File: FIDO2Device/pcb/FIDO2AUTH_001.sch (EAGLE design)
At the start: 1 part, among them U1 MDBT50Q-P1M

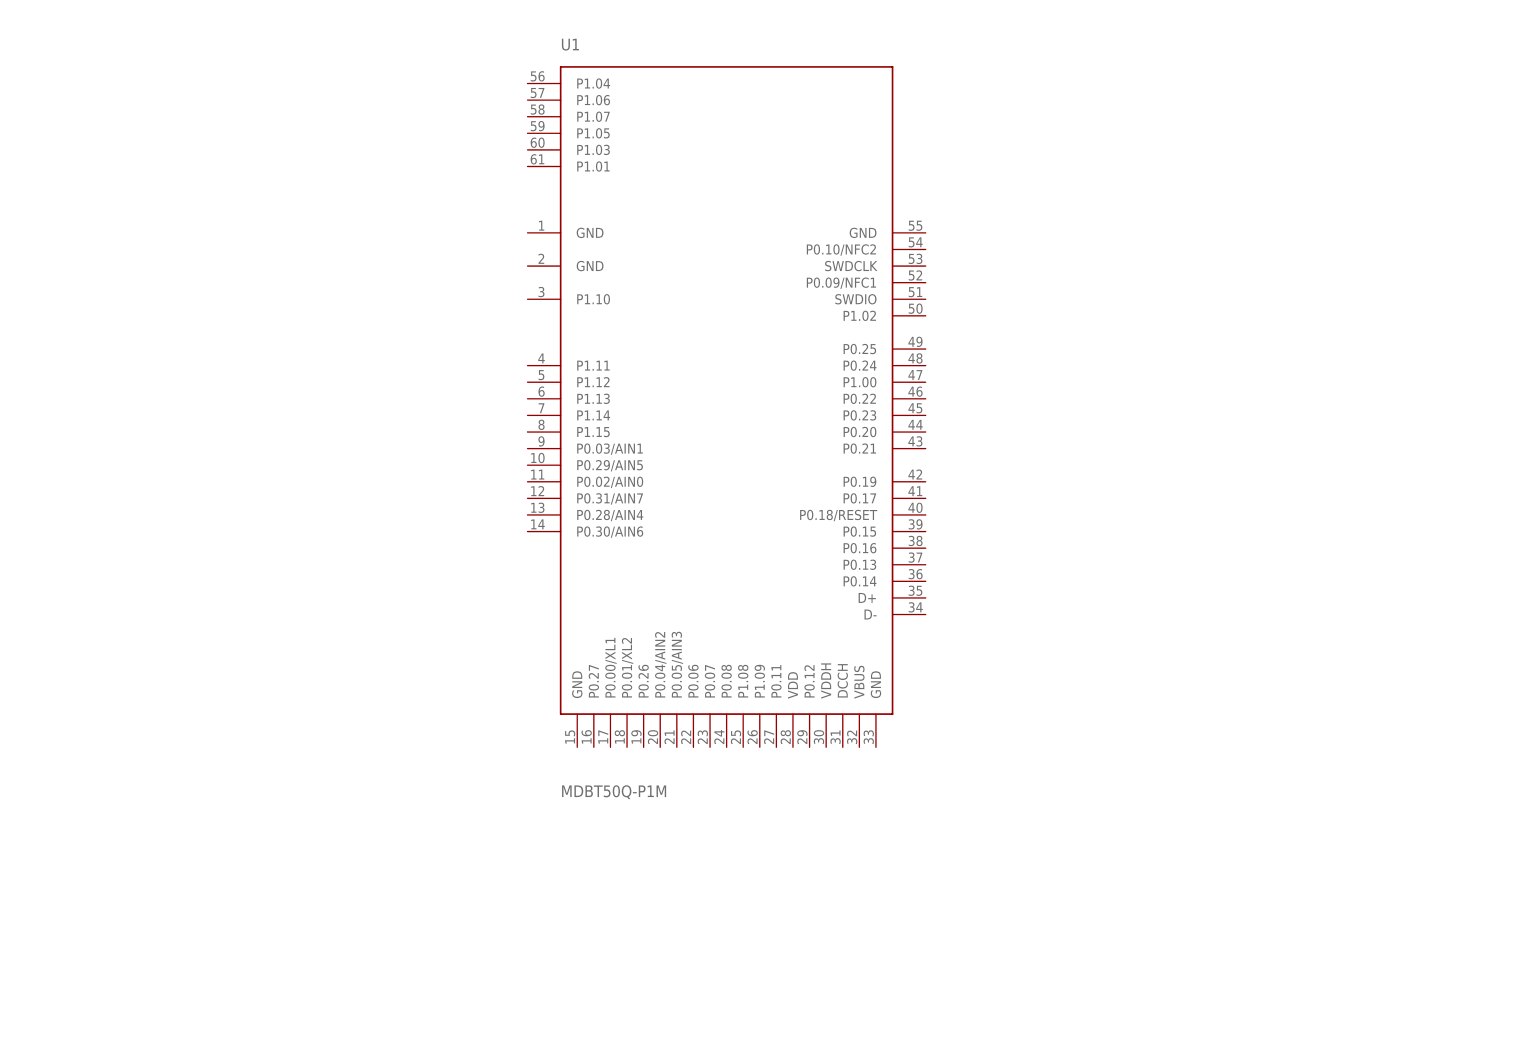
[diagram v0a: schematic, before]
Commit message: [WIP] ブレークアウト基板回路図
・クリスタル、バイパスコンデンサーを追加配置
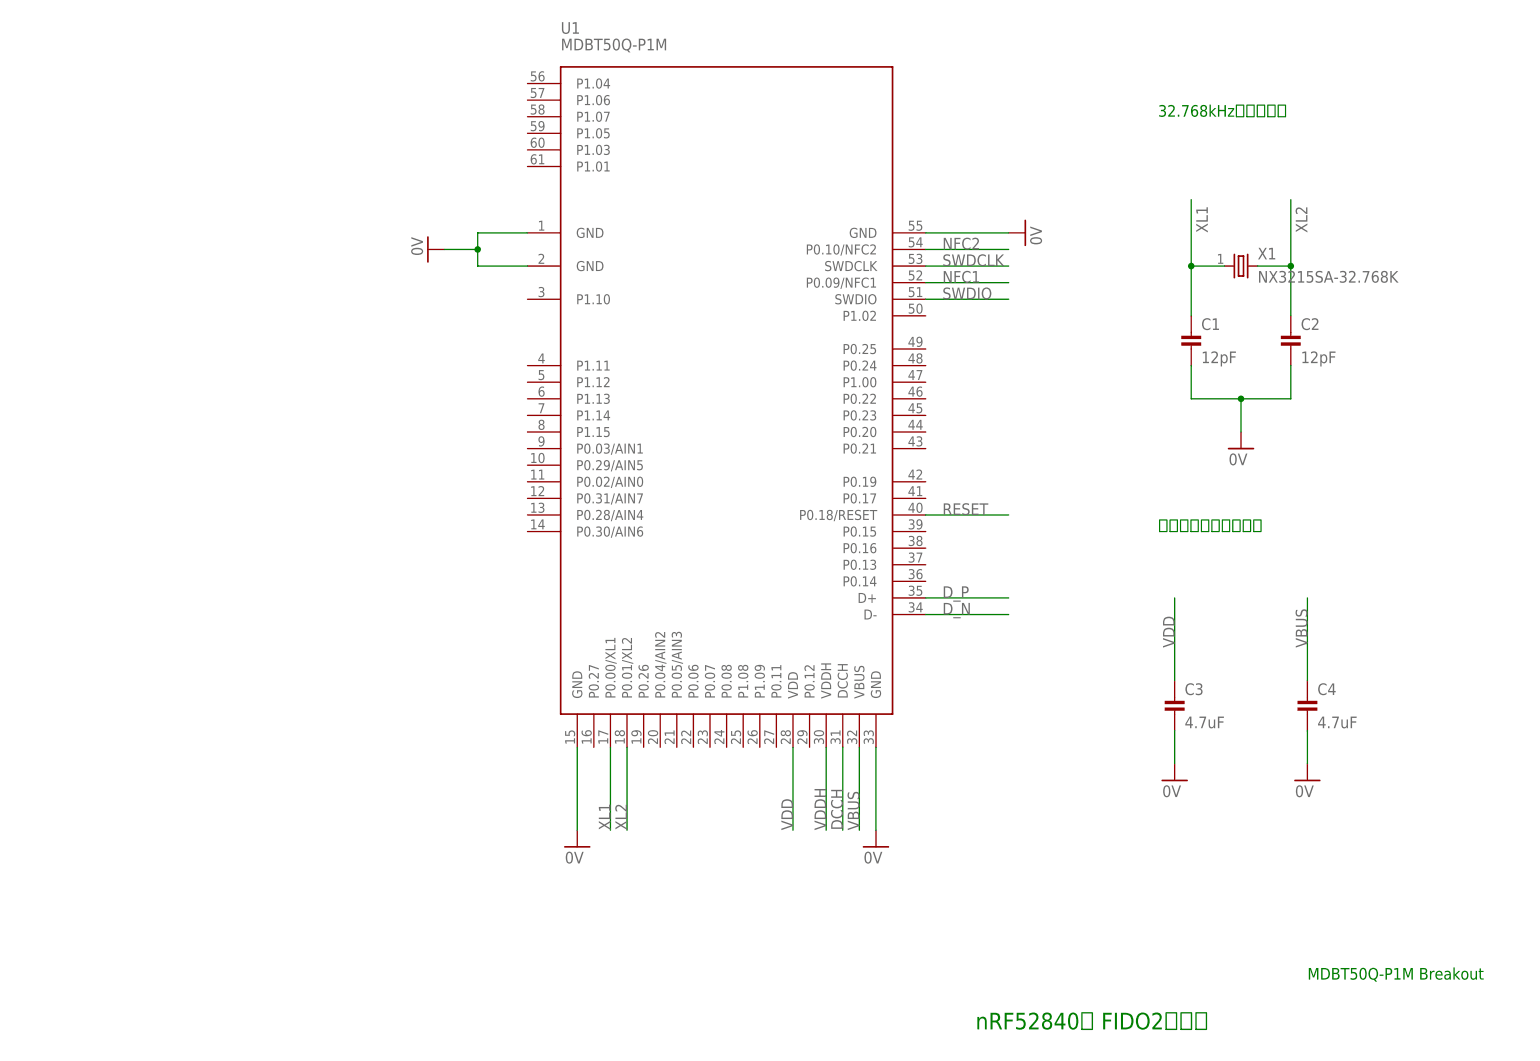
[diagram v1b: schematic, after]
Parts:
- added C1, C2: 12pF, Parts:CAP_0603
- added C3, C4: 4.7uF, Parts:CAP_0603
- added X1: NX3215SA-32.768K, Parts:NX3215SA-32.768K
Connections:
- new net 0V: C1.2, C2.2, C3.2, C4.2, U1.GND@1, U1.GND@15, U1.GND@2, U1.GND@33, U1.GND@55
- new net DCCH: U1.DCCH
- new net D_N: U1.D-
- new net D_P: U1.D+
- new net NFC1: U1.P0.09/NFC1
- new net NFC2: U1.P0.10/NFC2
- new net RESET: U1.P0.18/RESET
- new net SWDCLK: U1.SWDCLK
- new net SWDIO: U1.SWDIO
- new net VBUS: C4.1, U1.VBUS
- new net VDD: C3.1, U1.VDD
- new net VDDH: U1.VDDH
- new net XL1: C1.1, U1.P0.00/XL1, X1.1
- new net XL2: C2.1, U1.P0.01/XL2, X1.2
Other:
- note added: "32.768kHzクリスタル"
- note added: "MDBT50Q-P1M Breakout"
- note added: "nRF52840版 FIDO2認証器"
- note added: "バイパスコンデンサー"
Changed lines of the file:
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@@
 <setting verticaltext="up"/>
 </settings>
-<grid distance="0.1" unitdist="inch" unit="inch" style="lines" multiple="1" display="no" altdistance="0.01" altunitdist="inch" altunit="inch"/>
+<grid distance="0.1" unitdist="inch" unit="inch" style="lines" multiple="1" display="yes" altdistance="0.01" altunitdist="inch" altunit="inch"/>
 <layers>
 <layer number="1" name="Top" color="4" fill="1" visible="no" active="no"/>
@@
 <part name="U1" library="Parts" deviceset="MDBT50Q-P1M" device=""/>
 <part name="FRAME1" library="Generic" deviceset="A4L-LOC" device=""/>
+<part name="X1" library="Parts" deviceset="NX3215SA" device="-32.768K"/>
+<part name="C1" library="Parts" deviceset="CAP" device="_0603" value="12pF"/>
+<part name="C2" library="Parts" deviceset="CAP" device="_0603" value="12pF"/>
+<part name="GND1" library="Supply" deviceset="0V" device=""/>
+<part name="C3" library="Parts" deviceset="CAP" device="_0603" value="4.7uF"/>
+<part name="C4" library="Parts" deviceset="CAP" device="_0603" value="4.7uF"/>
+<part name="GND2" library="Supply" deviceset="0V" device=""/>
+<part name="GND3" library="Supply" deviceset="0V" device=""/>
+<part name="GND4" library="Supply" deviceset="0V" device=""/>
+<part name="GND5" library="Supply" deviceset="0V" device=""/>
+<part name="GND6" library="Supply" deviceset="0V" device=""/>
+<part name="GND7" library="Supply" deviceset="0V" device=""/>
 </parts>
 <sheets>
 <sheet>
 <plain>
+<text x="195.58" y="152.4" size="1.778" layer="91">32.768kHzクリスタル</text>
+<text x="195.58" y="88.9" size="1.778" layer="91">バイパスコンデンサー</text>
+<text x="218.44" y="20.32" size="1.778" layer="91">MDBT50Q-P1M Breakout</text>
+<text x="167.64" y="12.7" size="2.54" layer="91">nRF52840版 FIDO2認証器</text>
 </plain>
 <instances>
-<instance part="U1" gate="G$1" x="129.54" y="106.68"/>
+<instance part="U1" gate="G$1" x="129.54" y="106.68" smashed="yes">
+<attribute name="NAME" x="104.14" y="165.1" size="1.778" layer="95"/>
+<attribute name="VALUE" x="104.14" y="162.56" size="1.778" layer="96"/>
+</instance>
 <instance part="FRAME1" gate="G$1" x="0" y="0"/>
+<instance part="X1" gate="G$1" x="208.28" y="129.54"/>
+<instance part="C1" gate="G$1" x="200.66" y="121.92"/>
+<instance part="C2" gate="G$1" x="215.9" y="121.92"/>
+<instance part="GND1" gate="1" x="208.28" y="101.6"/>
+<instance part="C3" gate="G$1" x="198.12" y="66.04"/>
+<instance part="C4" gate="G$1" x="218.44" y="66.04"/>
+<instance part="GND2" gate="1" x="198.12" y="50.8"/>
+<instance part="GND3" gate="1" x="218.44" y="50.8"/>
+<instance part="GND4" gate="1" x="152.4" y="40.64"/>
+<instance part="GND5" gate="1" x="175.26" y="134.62" rot="R90"/>
+<instance part="GND6" gate="1" x="83.82" y="132.08" rot="R270"/>
+<instance part="GND7" gate="1" x="106.68" y="40.64"/>
 </instances>
 <busses>
 </busses>
 <nets>
+<net name="0V" class="0">
+<segment>
+<pinref part="C1" gate="G$1" pin="2"/>
+<wire x1="200.66" y1="114.3" x2="200.66" y2="109.22" width="0.1524" layer="91"/>
+<pinref part="GND1" gate="1" pin="0V"/>
+<wire x1="200.66" y1="109.22" x2="208.28" y2="109.22" width="0.1524" layer="91"/>
+<wire x1="208.28" y1="109.22" x2="208.28" y2="104.14" width="0.1524" layer="91"/>
+<wire x1="208.28" y1="109.22" x2="215.9" y2="109.22" width="0.1524" layer="91"/>
+<junction x="208.28" y="109.22"/>
+<pinref part="C2" gate="G$1" pin="2"/>
+<wire x1="215.9" y1="109.22" x2="215.9" y2="114.3" width="0.1524" layer="91"/>
+</segment>
+<segment>
+<pinref part="GND2" gate="1" pin="0V"/>
+<pinref part="C3" gate="G$1" pin="2"/>
+<wire x1="198.12" y1="53.34" x2="198.12" y2="58.42" width="0.1524" layer="91"/>
+</segment>
+<segment>
+<pinref part="GND3" gate="1" pin="0V"/>
+<pinref part="C4" gate="G$1" pin="2"/>
+<wire x1="218.44" y1="53.34" x2="218.44" y2="58.42" width="0.1524" layer="91"/>
+</segment>
+<segment>
+<pinref part="U1" gate="G$1" pin="GND@15"/>
+<pinref part="GND7" gate="1" pin="0V"/>
+<wire x1="106.68" y1="55.88" x2="106.68" y2="43.18" width="0.1524" layer="91"/>
+</segment>
+<segment>
+<pinref part="U1" gate="G$1" pin="GND@33"/>
+<pinref part="GND4" gate="1" pin="0V"/>
+<wire x1="152.4" y1="55.88" x2="152.4" y2="43.18" width="0.1524" layer="91"/>
+</segment>
+<segment>
+<pinref part="U1" gate="G$1" pin="GND@55"/>
+<pinref part="GND5" gate="1" pin="0V"/>
+<wire x1="160.02" y1="134.62" x2="172.72" y2="134.62" width="0.1524" layer="91"/>
+</segment>
+<segment>
+<pinref part="U1" gate="G$1" pin="GND@1"/>
+<wire x1="99.06" y1="134.62" x2="91.44" y2="134.62" width="0.1524" layer="91"/>
+<wire x1="91.44" y1="134.62" x2="91.44" y2="132.08" width="0.1524" layer="91"/>
+<pinref part="GND6" gate="1" pin="0V"/>
+<wire x1="91.44" y1="132.08" x2="86.36" y2="132.08" width="0.1524" layer="91"/>
+<pinref part="U1" gate="G$1" pin="GND@2"/>
+<wire x1="99.06" y1="129.54" x2="91.44" y2="129.54" width="0.1524" layer="91"/>
+<wire x1="91.44" y1="129.54" x2="91.44" y2="132.08" width="0.1524" layer="91"/>
+<junction x="91.44" y="132.08"/>
+</segment>
+</net>
+<net name="XL1" class="0">
+<segment>
+<pinref part="X1" gate="G$1" pin="1"/>
+<wire x1="205.74" y1="129.54" x2="200.66" y2="129.54" width="0.1524" layer="91"/>
+<pinref part="C1" gate="G$1" pin="1"/>
+<wire x1="200.66" y1="129.54" x2="200.66" y2="121.92" width="0.1524" layer="91"/>
+<wire x1="200.66" y1="129.54" x2="200.66" y2="139.7" width="0.1524" layer="91"/>
+<junction x="200.66" y="129.54"/>
+<label x="203.2" y="134.62" size="1.778" layer="95" rot="R90"/>
+</segment>
+<segment>
+<pinref part="U1" gate="G$1" pin="P0.00/XL1"/>
+<wire x1="111.76" y1="55.88" x2="111.76" y2="43.18" width="0.1524" layer="91"/>
+<label x="111.76" y="43.18" size="1.778" layer="95" rot="R90"/>
+</segment>
+</net>
+<net name="XL2" class="0">
+<segment>
+<pinref part="X1" gate="G$1" pin="2"/>
+<pinref part="C2" gate="G$1" pin="1"/>
+<wire x1="210.82" y1="129.54" x2="215.9" y2="129.54" width="0.1524" layer="91"/>
+<wire x1="215.9" y1="129.54" x2="215.9" y2="121.92" width="0.1524" layer="91"/>
+<wire x1="215.9" y1="129.54" x2="215.9" y2="139.7" width="0.1524" layer="91"/>
+<junction x="215.9" y="129.54"/>
+<label x="218.44" y="134.62" size="1.778" layer="95" rot="R90"/>
+</segment>
+<segment>
+<pinref part="U1" gate="G$1" pin="P0.01/XL2"/>
+<wire x1="114.3" y1="55.88" x2="114.3" y2="43.18" width="0.1524" layer="91"/>
+<label x="114.3" y="43.18" size="1.778" layer="95" rot="R90"/>
+</segment>
+</net>
+<net name="VDD" class="0">
+<segment>
+<pinref part="C3" gate="G$1" pin="1"/>
+<wire x1="198.12" y1="66.04" x2="198.12" y2="78.74" width="0.1524" layer="91"/>
+<label x="198.12" y="71.12" size="1.778" layer="95" rot="R90"/>
+</segment>
+<segment>
+<pinref part="U1" gate="G$1" pin="VDD"/>
+<wire x1="139.7" y1="55.88" x2="139.7" y2="43.18" width="0.1524" layer="91"/>
+<label x="139.7" y="43.18" size="1.778" layer="95" rot="R90"/>
+</segment>
+</net>
+<net name="VBUS" class="0">
+<segment>
+<pinref part="C4" gate="G$1" pin="1"/>
+<wire x1="218.44" y1="66.04" x2="218.44" y2="78.74" width="0.1524" layer="91"/>
+<label x="218.44" y="71.12" size="1.778" layer="95" rot="R90"/>
+</segment>
+<segment>
+<pinref part="U1" gate="G$1" pin="VBUS"/>
+<wire x1="149.86" y1="55.88" x2="149.86" y2="43.18" width="0.1524" layer="91"/>
+<label x="149.86" y="43.18" size="1.778" layer="95" rot="R90"/>
+</segment>
+</net>
+<net name="SWDCLK" class="0">
+<segment>
+<pinref part="U1" gate="G$1" pin="SWDCLK"/>
+<wire x1="160.02" y1="129.54" x2="172.72" y2="129.54" width="0.1524" layer="91"/>
+<label x="162.56" y="129.54" size="1.778" layer="95"/>
+</segment>
+</net>
+<net name="NFC1" class="0">
+<segment>
+<pinref part="U1" gate="G$1" pin="P0.09/NFC1"/>
+<wire x1="160.02" y1="127" x2="172.72" y2="127" width="0.1524" layer="91"/>
+<label x="162.56" y="127" size="1.778" layer="95"/>
+</segment>
+</net>
+<net name="NFC2" class="0">
+<segment>
+<pinref part="U1" gate="G$1" pin="P0.10/NFC2"/>
+<wire x1="160.02" y1="132.08" x2="172.72" y2="132.08" width="0.1524" layer="91"/>
+<label x="162.56" y="132.08" size="1.778" layer="95"/>
+</segment>
+</net>
+<net name="SWDIO" class="0">
+<segment>
+<pinref part="U1" gate="G$1" pin="SWDIO"/>
+<wire x1="160.02" y1="124.46" x2="172.72" y2="124.46" width="0.1524" layer="91"/>
+<label x="162.56" y="124.46" size="1.778" layer="95"/>
+</segment>
+</net>
+<net name="RESET" class="0">
+<segment>
+<pinref part="U1" gate="G$1" pin="P0.18/RESET"/>
+<wire x1="160.02" y1="91.44" x2="172.72" y2="91.44" width="0.1524" layer="91"/>
+<label x="162.56" y="91.44" size="1.778" layer="95"/>
+</segment>
+</net>
+<net name="D_P" class="0">
+<segment>
+<pinref part="U1" gate="G$1" pin="D+"/>
+<wire x1="160.02" y1="78.74" x2="172.72" y2="78.74" width="0.1524" layer="91"/>
+<label x="162.56" y="78.74" size="1.778" layer="95"/>
+</segment>
+</net>
+<net name="D_N" class="0">
+<segment>
+<pinref part="U1" gate="G$1" pin="D-"/>
+<wire x1="160.02" y1="76.2" x2="172.72" y2="76.2" width="0.1524" layer="91"/>
+<label x="162.56" y="76.2" size="1.778" layer="95"/>
+</segment>
+</net>
+<net name="VDDH" class="0">
+<segment>
+<pinref part="U1" gate="G$1" pin="VDDH"/>
+<wire x1="144.78" y1="55.88" x2="144.78" y2="43.18" width="0.1524" layer="91"/>
+<label x="144.78" y="43.18" size="1.778" layer="95" rot="R90"/>
+</segment>
+</net>
+<net name="DCCH" class="0">
+<segment>
+<pinref part="U1" gate="G$1" pin="DCCH"/>
+<wire x1="147.32" y1="55.88" x2="147.32" y2="43.18" width="0.1524" layer="91"/>
+<label x="147.32" y="43.18" size="1.778" layer="95" rot="R90"/>
+</segment>
+</net>
 </nets>
 </sheet>

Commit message: [WIP] ブレークアウト基板回路図
・USBプラグ部を追加
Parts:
- added C5, C6: 10uF, Parts:CAP_0603
- added C7, C8: 0.1uF, Parts:CAP_0402
- added CN1: TE-1734028, Connectors:TE-1734028
- added D1: PRTR5V0U2X, Parts:PRTR5V0U2X
- added FB1, FB2, FB3: BLM15AG121SN1D, Parts:BLM15AG121SN1D
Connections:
- removed net DCCH: U1.DCCH
- removed net VBUS: C4.1, U1.VBUS
- removed net VDD: C3.1, U1.VDD
- removed net VDDH: U1.VDDH
- new net N$1: C5.1, C6.1, C8.1, CN1.VBUS, D1.VCC, FB1.1
- new net N$2: CN1.GND, FB2.1
- new net N$3: CN1.FG1, CN1.FG2, FB3.1
- new net VBUS_NRF: C4.1, C7.1, FB1.2, U1.VBUS
- new net VDD_NRF: C3.1, U1.VDD, U1.VDDH
- net 0V: now also C5.2, C6.2, C7.2, C8.2, D1.GND, FB2.2, FB3.2
- net D_N: now also CN1.D-, D1.I/O_1
- net D_P: now also CN1.D+, D1.I/O_2
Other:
- note added: "USBプラグ部"
- note added: "nRF52840"
- note added: "モジュール部"
- note removed: "nRF52840版 FIDO2認証器"

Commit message: [WIP] ブレークアウト基板回路図
・リセット回路、MAIN SWを追加
・回路図プレビュー、プリント基板配置イメージを追加
・電源供給／プログラミング／GPIOの各ピンをインターフェースするための機構は後日追加予定です。
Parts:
- added C9: 0.1uF, Parts:CAP_0402
- added R1: 10k, Parts:RESISTOR_0402
- added SB1: (no value), Connectors:SJ
- added SW1: SKRPACE010, Parts:SKRPACE010
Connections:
- new net LED1: U1.P0.06
- new net LED2_B: U1.P0.12
- new net LED2_G: U1.P1.09
- new net LED2_R: U1.P0.08
- new net SW1: SW1.P, SW1.P1, U1.P1.06
- net 0V: now also C9.2, SB1.1, SW1.S, SW1.S1
- net RESET: now also C9.1, R1.2, SB1.2
- net VDD_NRF: now also R1.1
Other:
- note added: "MAIN SW"
- note added: "nRF52840版FIDO2認証器 開発用ブレークアウト基板"
- note added: "ジャンパーをショートすると リセットがかかります。"
- note added: "リセット回路"
- note removed: "nRF52840"
- moved on the sheet: C1, C2, C3, C4, X1
